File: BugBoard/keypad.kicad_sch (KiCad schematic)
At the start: 17 parts, among them J1 USB_B_Micro, J4 Conn_01x06_Pin, SW1 Ident, U1 PY32F003F18P6TU, U3 XC6206P332MR, U4 NRF24L01_SMD, U5 CH330N

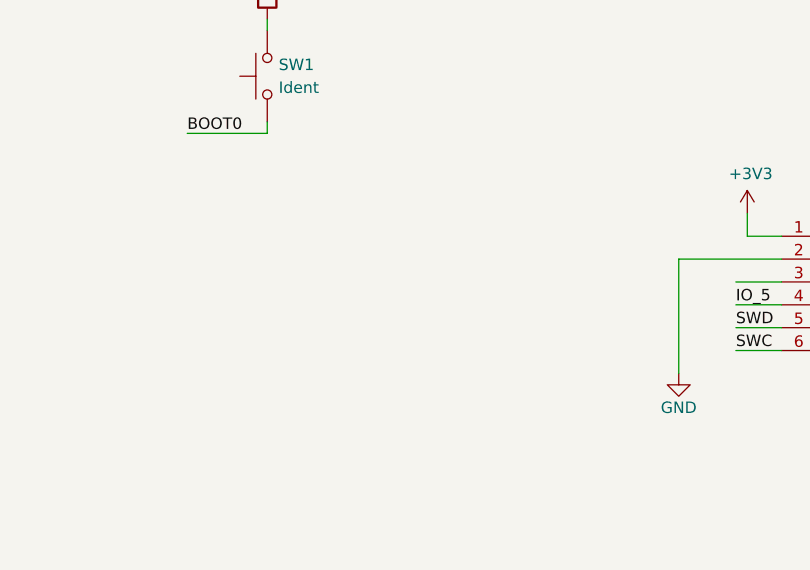
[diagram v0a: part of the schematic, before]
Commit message: Added JST i2c connector
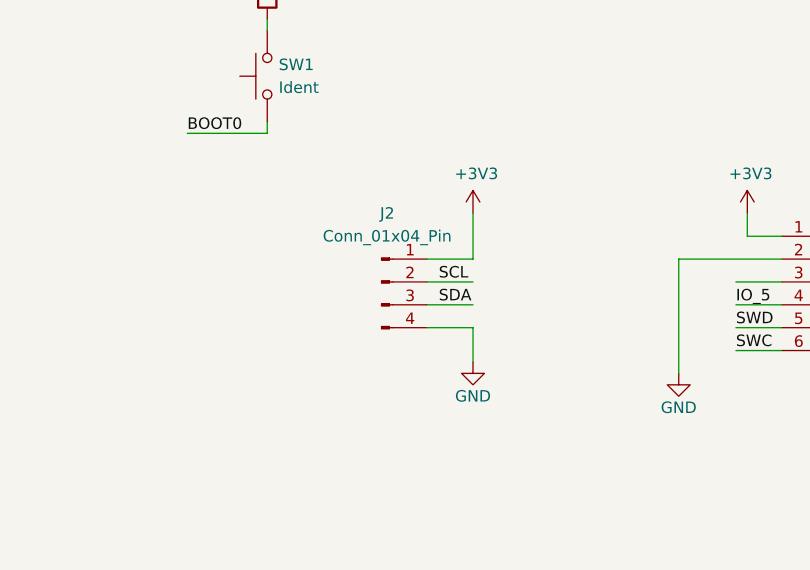
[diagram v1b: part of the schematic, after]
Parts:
- added J2: Conn_01x04_Pin, Connector_JST:JST_GH_SM04B-GHS-TB_1x04-1MP_P1.25mm_Horizontal, symbol Connector:Conn_01x04_Pin
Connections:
- net +3V3: now also J2.1 (Pin_1)
- net GND: now also J2.4 (Pin_4)
- net SCL: now also J2.2 (Pin_2)
- net SDA: now also J2.3 (Pin_3)
